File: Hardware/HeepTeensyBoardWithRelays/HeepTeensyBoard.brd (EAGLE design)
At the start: 100 x 54 mm, 43 parts, among them J1 MAGJACK, J4 POWER_JACKPTH, K1 RELAY-SPDT-JZC-11F, K2 RELAY-SPDT-JZC-11F, K3 RELAY-SPDT-JZC-11F, Q1 25MHz, U1 ENC28J60-SO

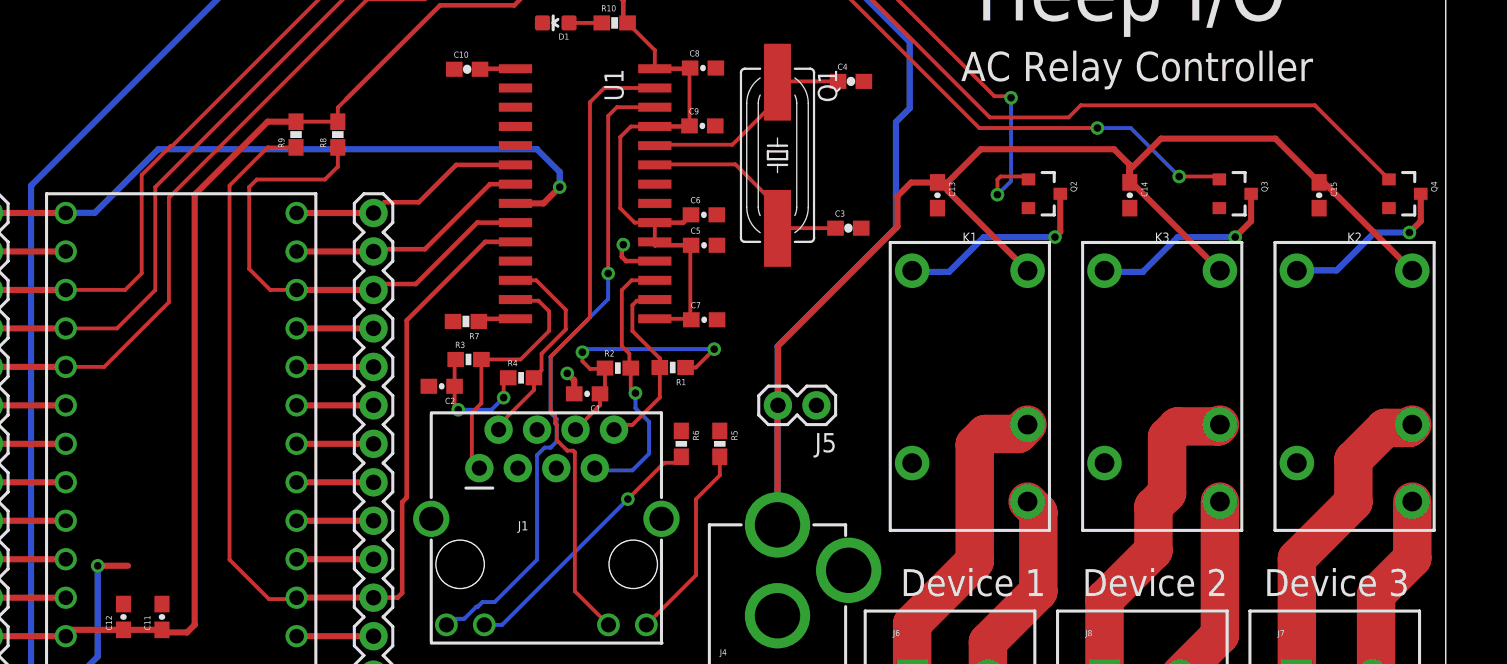
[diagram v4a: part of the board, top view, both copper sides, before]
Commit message: #152 Removed all DRC errors
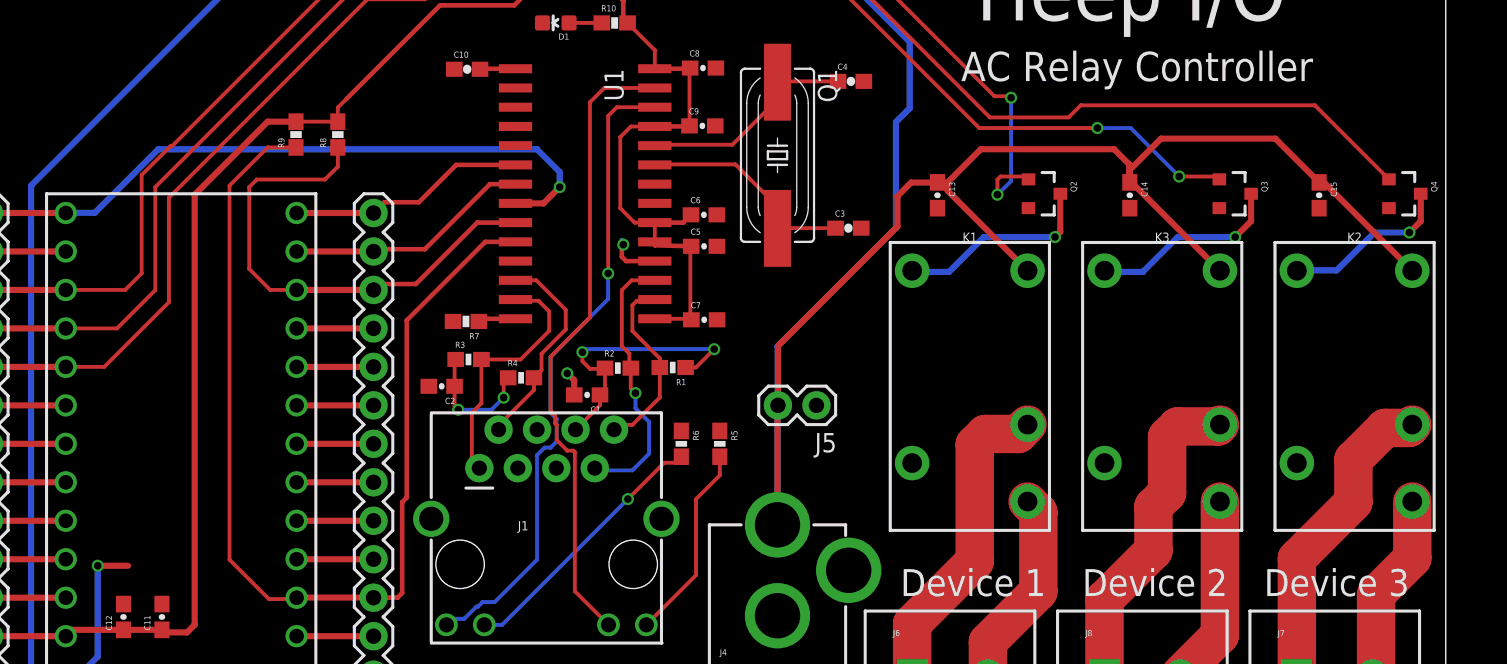
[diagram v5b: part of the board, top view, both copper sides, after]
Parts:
- moved C1 0.07 mm to (43.3, 22.3)
- moved C5 0.07 mm to (51.0, 32.1)
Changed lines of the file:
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@@
 <setting verticaltext="up"/>
 </settings>
-<grid distance="1" unitdist="mm" unit="mm" style="lines" multiple="1" display="no" altdistance="0.025" altunitdist="inch" altunit="inch"/>
+<grid distance="0.01" unitdist="mm" unit="mm" style="lines" multiple="1" display="no" altdistance="0.025" altunitdist="inch" altunit="inch"/>
 <layers>
 <layer number="1" name="Top" color="4" fill="1" visible="yes" active="yes"/>
@@
 </class>
 </classes>
-<designrules name="default">
+<designrules name="SeeedStudio_2layer_DRU_no_angle_20140221">
 <description language="de">&lt;b&gt;EAGLE Design Rules&lt;/b&gt;
 &lt;p&gt;
@@
 necessary adjustments and save your customized
 design rules under a new name.</description>
+<description language="zh">&lt;b&gt;Seeed Studio EAGLE Design Rules&lt;/b&gt;
+</description>
 <param name="layerSetup" value="(1*16)"/>
-<param name="mtCopper" value="0.035mm 0.035mm 0.035mm 0.035mm 0.035mm 0.035mm 0.035mm 0.035mm 0.035mm 0.035mm 0.035mm 0.035mm 0.035mm 0.035mm 0.035mm 0.035mm"/>
-<param name="mtIsolate" value="1.5mm 0.15mm 0.2mm 0.15mm 0.2mm 0.15mm 0.2mm 0.15mm 0.2mm 0.15mm 0.2mm 0.15mm 0.2mm 0.15mm 0.2mm"/>
-<param name="mdWireWire" value="8mil"/>
-<param name="mdWirePad" value="8mil"/>
-<param name="mdWireVia" value="8mil"/>
-<param name="mdPadPad" value="8mil"/>
-<param name="mdPadVia" value="8mil"/>
-<param name="mdViaVia" value="8mil"/>
-<param name="mdSmdPad" value="8mil"/>
-<param name="mdSmdVia" value="8mil"/>
-<param name="mdSmdSmd" value="8mil"/>
+<param name="mtCopper" value="0.035mm 0.0175mm 0.035mm 0.035mm 0.035mm 0.035mm 0.035mm 0.035mm 0.035mm 0.035mm 0.035mm 0.035mm 0.035mm 0.035mm 0.0175mm 0.035mm"/>
+<param name="mtIsolate" value="1.5mm 1.1mm 0.2mm 0.15mm 0.2mm 0.15mm 0.2mm 0.15mm 0.2mm 0.15mm 0.2mm 0.15mm 0.2mm 0.15mm 0.2mm"/>
+<param name="mdWireWire" value="6mil"/>
+<param name="mdWirePad" value="6mil"/>
+<param name="mdWireVia" value="6mil"/>
+<param name="mdPadPad" value="6mil"/>
+<param name="mdPadVia" value="6mil"/>
+<param name="mdViaVia" value="6mil"/>
+<param name="mdSmdPad" value="0mil"/>
+<param name="mdSmdVia" value="0mil"/>
+<param name="mdSmdSmd" value="0mil"/>
 <param name="mdViaViaSameLayer" value="8mil"/>
 <param name="mnLayersViaInSmd" value="2"/>
-<param name="mdCopperDimension" value="40mil"/>
-<param name="mdDrill" value="8mil"/>
+<param name="mdCopperDimension" value="10mil"/>
+<param name="mdDrill" value="10mil"/>
 <param name="mdSmdStop" value="0mil"/>
-<param name="msWidth" value="10mil"/>
-<param name="msDrill" value="24mil"/>
-<param name="msMicroVia" value="9.99mm"/>
+<param name="msWidth" value="6mil"/>
+<param name="msDrill" value="12mil"/>
+<param name="msMicroVia" value="12mil"/>
 <param name="msBlindViaRatio" value="0.5"/>
 <param name="rvPadTop" value="0.25"/>
@@
 <param name="rlMinPadBottom" value="10mil"/>
 <param name="rlMaxPadBottom" value="20mil"/>
-<param name="rlMinViaOuter" value="8mil"/>
+<param name="rlMinViaOuter" value="6mil"/>
 <param name="rlMaxViaOuter" value="20mil"/>
-<param name="rlMinViaInner" value="8mil"/>
+<param name="rlMinViaInner" value="6mil"/>
 <param name="rlMaxViaInner" value="20mil"/>
 <param name="rlMinMicroViaOuter" value="4mil"/>
@@
 <param name="psTop" value="-1"/>
 <param name="psBottom" value="-1"/>
-<param name="psFirst" value="-1"/>
+<param name="psFirst" value="0"/>
 <param name="psElongationLong" value="100"/>
 <param name="psElongationOffset" value="100"/>
 <param name="mvStopFrame" value="1"/>
 <param name="mvCreamFrame" value="0"/>
-<param name="mlMinStopFrame" value="4mil"/>
-<param name="mlMaxStopFrame" value="4mil"/>
+<param name="mlMinStopFrame" value="2mil"/>
+<param name="mlMaxStopFrame" value="2mil"/>
 <param name="mlMinCreamFrame" value="0mil"/>
 <param name="mlMaxCreamFrame" value="0mil"/>
-<param name="mlViaStopLimit" value="0mil"/>
+<param name="mlViaStopLimit" value="100mil"/>
 <param name="srRoundness" value="0"/>
 <param name="srMinRoundness" value="0mil"/>
@@
 <param name="checkAngle" value="0"/>
 <param name="checkFont" value="1"/>
-<param name="checkRestrict" value="1"/>
+<param name="checkRestrict" value="0"/>
 <param name="useDiameter" value="13"/>
 <param name="maxErrors" value="50"/>
@@
 </autorouter>
 <elements>
-<element name="C1" library="SparkFun-Capacitors" package="0603-CAP" value="0.1uF" x="43.31" y="22.35" rot="R180"/>
+<element name="C1" library="SparkFun-Capacitors" package="0603-CAP" value="0.1uF" x="43.31" y="22.28" rot="R180"/>
 <element name="C10" library="SparkFun-Passives" package="0603-CAP" value="10uF" x="35.39" y="43.78"/>
 <element name="C11" library="SparkFun-Capacitors" package="0603-CAP" value="0.1uF" x="15.24" y="7.62" rot="R90"/>
@@
 <element name="C3" library="SparkFun-Passives" package="0603-CAP" value="10pF" x="60.56" y="33.29"/>
 <element name="C4" library="SparkFun-Passives" package="0603-CAP" value="10pF" x="60.73" y="42.98"/>
-<element name="C5" library="SparkFun-Capacitors" package="0603-CAP" value="0.1uF" x="51.03" y="32.16"/>
+<element name="C5" library="SparkFun-Capacitors" package="0603-CAP" value="0.1uF" x="51.03" y="32.09"/>
 <element name="C6" library="SparkFun-Capacitors" package="0603-CAP" value="0.1uF" x="51.02" y="34.17"/>
 <element name="C7" library="SparkFun-Capacitors" package="0603-CAP" value="0.1uF" x="51.04" y="27.24"/>
@@
 <contactref element="J1" pad="6"/>
 <wire x1="44.49" y1="24.05" x2="44.49" y2="22.68" width="0.254" layer="1"/>
-<wire x1="44.49" y1="22.68" x2="44.16" y2="22.35" width="0.254" layer="1"/>
-<wire x1="44.16" y1="22.35" x2="44.16" y2="21.6" width="0.254" layer="1"/>
+<wire x1="44.49" y1="22.68" x2="44.16" y2="22.28" width="0.254" layer="1"/>
+<wire x1="44.16" y1="22.28" x2="44.16" y2="21.6" width="0.254" layer="1"/>
 <wire x1="44.16" y1="21.6" x2="42.545" y2="19.985" width="0.254" layer="1"/>
 <wire x1="49.81" y1="24.09" x2="50.49" y2="24.09" width="0.254" layer="1"/>
@@
 <wire x1="45.7" y1="32.2" x2="45.7" y2="32.4" width="0.3048" layer="16"/>
 <wire x1="45.7" y1="32.4" x2="45.6" y2="32.5" width="0.3048" layer="16"/>
-<wire x1="42.46" y1="22.35" x2="42.46" y2="23.24" width="0.4064" layer="1"/>
+<wire x1="42.46" y1="22.28" x2="42.46" y2="23.24" width="0.4064" layer="1"/>
 <wire x1="42.46" y1="23.24" x2="42" y2="23.7" width="0.4064" layer="1"/>
 <via x="42" y="23.7" extent="1-16" drill="0.5" shape="square"/>
@@
 <wire x1="47.78" y1="40.005" x2="50.07" y2="40.005" width="0.3048" layer="1"/>
 <wire x1="50.07" y1="40.005" x2="50.07" y2="40.04" width="0.3048" layer="1"/>
-<wire x1="50.18" y1="32.16" x2="47.78" y2="32.16" width="0.3048" layer="1"/>
+<wire x1="50.18" y1="32.09" x2="47.78" y2="32.16" width="0.3048" layer="1"/>
 <wire x1="47.78" y1="32.16" x2="47.78" y2="32.385" width="0.3048" layer="1"/>
 <wire x1="47.78" y1="33.655" x2="49.655" y2="33.655" width="0.3048" layer="1"/>
@@
 <wire x1="47.78" y1="32.385" x2="47.78" y2="33.655" width="0.254" layer="1"/>
 <wire x1="50.125" y1="27.305" x2="50.125" y2="32.105" width="0.254" layer="1"/>
-<wire x1="50.125" y1="32.105" x2="50.18" y2="32.16" width="0.254" layer="1"/>
+<wire x1="50.125" y1="32.105" x2="50.18" y2="32.09" width="0.254" layer="1"/>
 <wire x1="47.78" y1="33.655" x2="46.445" y2="33.655" width="0.254" layer="1"/>
 <wire x1="46.445" y1="33.655" x2="45.5" y2="34.6" width="0.254" layer="1"/>

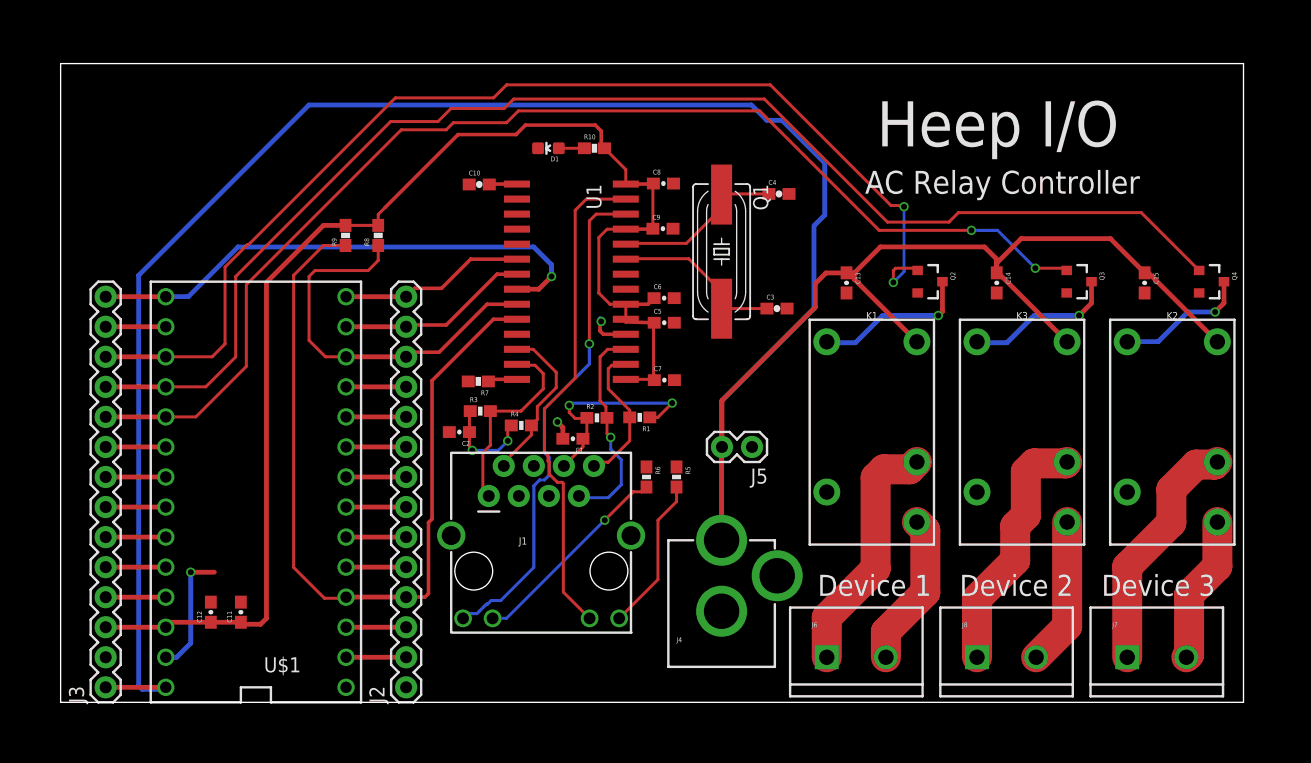
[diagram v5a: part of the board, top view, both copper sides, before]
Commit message: #152 Added kick back diodes to the relay circuits
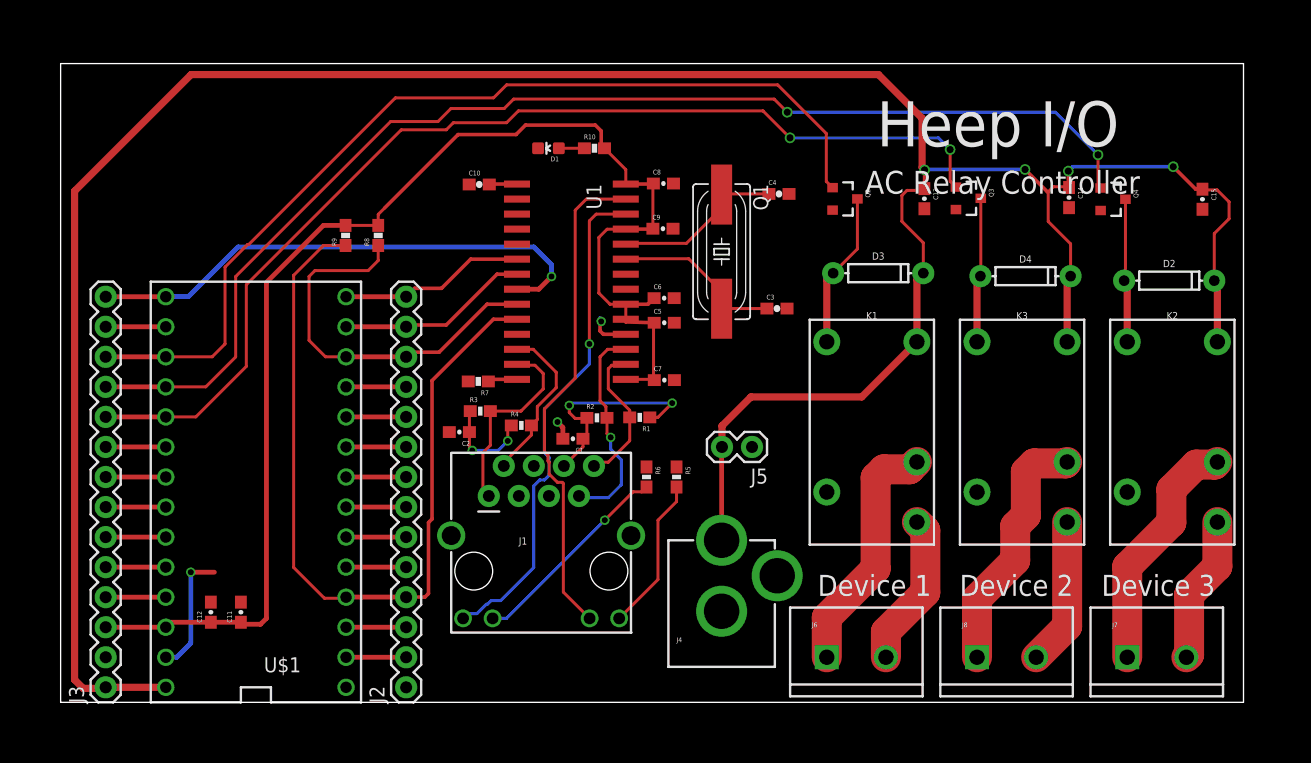
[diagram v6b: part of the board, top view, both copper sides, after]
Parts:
- added D2, D3, D4: 200mA/100V/1V, SparkFun-DiscreteSemi:DIODE-1N4148
- moved Q3 11.7 mm to (76.7, 42.6)
- moved Q4 10.9 mm to (88.9, 42.5)
- moved Q2 10.0 mm to (66.3, 42.6)
- moved C13 9.69 mm to (73.0, 42.6)
- moved C14 9.45 mm to (85.2, 42.7)
- moved C15 8.60 mm to (96.5, 42.5)
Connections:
- net N$11: now also D2.A
- net N$14: now also D4.A
- net N$9: now also D3.A
- net VIN: now also D2.C, D3.C, D4.C
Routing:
- net TEENSY15: track 95.1 -> 80.8 mm, vias 2 -> 0
- net TEENSY17: track 101.6 -> 90.9 mm
- net VIN: track 227.3 -> 238.0 mm, vias 0 -> 4
- net TEENSY16: track 113.2 -> 102.8 mm, vias 0 -> 2
- net N$11: track 11.3 -> 12.2 mm, vias 1 -> 0
- net N$14: track 12.9 -> 12.3 mm, vias 1 -> 0
- net N$9: track 13.4 -> 13.2 mm, vias 1 -> 0

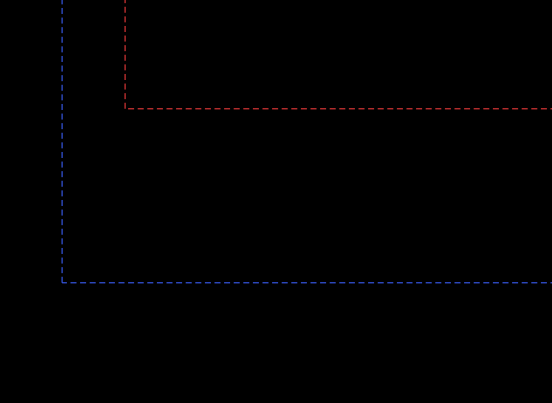
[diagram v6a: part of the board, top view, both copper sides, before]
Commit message: #156 Added ferrite bead to schematic
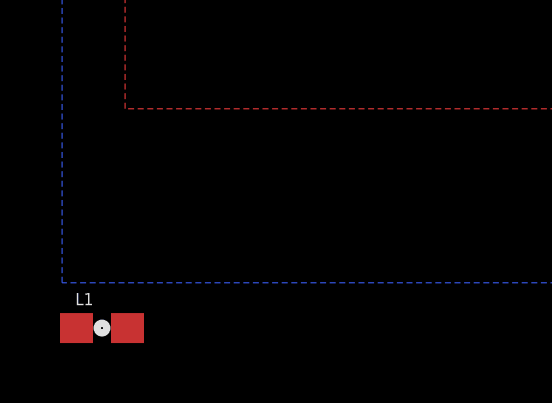
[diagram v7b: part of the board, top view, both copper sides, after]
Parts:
- added L1: (no value), SparkFun-Passives:0603
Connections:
- net 3.3V: now also L1.1
- net N$7: now also L1.2
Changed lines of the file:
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@@
 <attribute name="PROD_ID" value="DIO-08378" x="81.57" y="36.03" size="1.778" layer="27" display="off"/>
 </element>
+<element name="L1" library="SparkFun-Passives" package="0603" value="" x="-10.57" y="-18.51"/>
 </elements>
 <signals>
@@
 <wire x1="43.5" y1="24" x2="44.44" y2="24" width="0.254" layer="1"/>
 <wire x1="44.44" y1="24" x2="44.49" y2="24.05" width="0.254" layer="1"/>
+<contactref element="L1" pad="2"/>
+<wire x1="-9.72" y1="-18.51" x2="42.545" y2="19.985" width="0" layer="19" extent="1-1"/>
 </signal>
 <signal name="GND">
@@
 <wire x1="9.31" y1="6.77" x2="8.89" y2="6.35" width="0.4064" layer="1"/>
 <wire x1="8.89" y1="6.35" x2="3.81" y2="6.35" width="0.4064" layer="1"/>
+<contactref element="L1" pad="1"/>
+<wire x1="3.81" y1="6.35" x2="-11.42" y2="-18.51" width="0" layer="19" extent="1-1"/>
 </signal>
 <signal name="N$15">
